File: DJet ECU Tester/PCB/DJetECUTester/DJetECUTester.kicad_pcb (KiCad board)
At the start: 2 copper layers, 93 x 60 mm, 101 parts, among them J1 ISP, J2 ECU, J3 USB_B_Mini, J4 BREAKOUT, J5 12V IN, J6 MPS, J7 VAC, J8 INJECTORS, Q1 MMBT2222ALT1G, Q10 MMBT2222ALT1G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

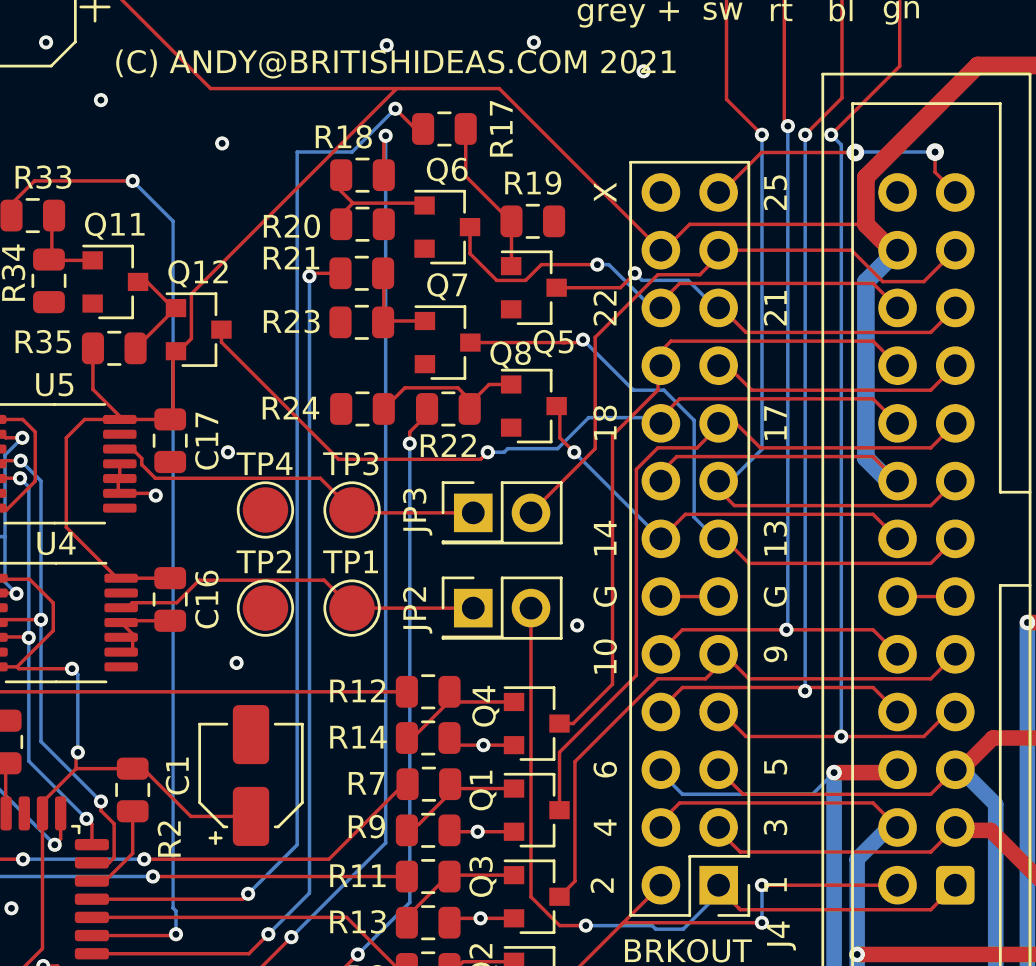
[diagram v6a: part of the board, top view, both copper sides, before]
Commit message: Added resistor to tester. Generated manufacturing files.
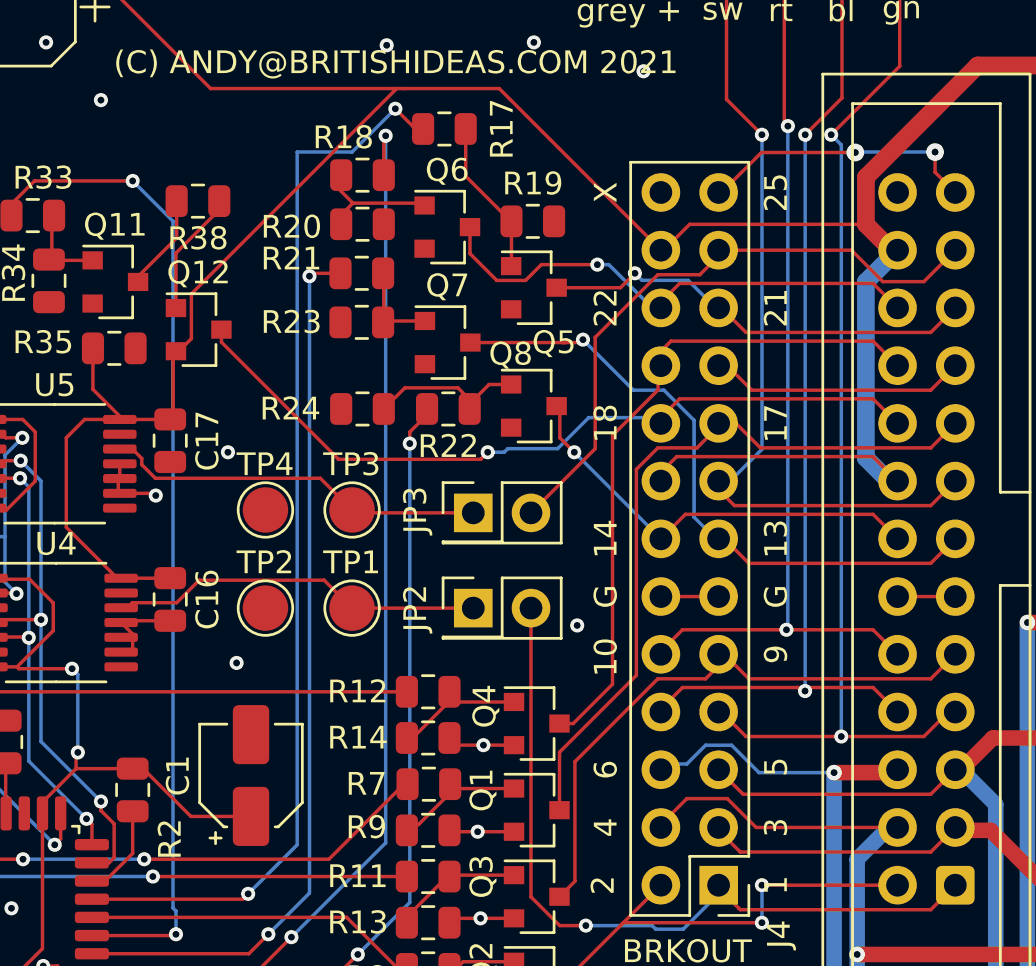
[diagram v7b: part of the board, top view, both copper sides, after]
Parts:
- added R38: 1k, Resistor_SMD:R_0805_2012Metric, F.Cu at (219.8, 83.9)
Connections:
- Q12 pad 1: Net-(Q11-Pad3) -> Net-(Q12-Pad1)
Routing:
- net Net-(Q12-Pad1): track 0.00 -> 4.93 mm
- net GND: vias 77 -> 76

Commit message: Working on version 1.1
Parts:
- removed JP1: RUN, Connector_PinHeader_2.54mm:PinHeader_1x02_P2.54mm_Vertical
- added J10: ECU3, Britishideas:PhoenixContact_COMBICON_PT_7, F.Cu at (264.0, 59.7)
- added J9: ECU2, Britishideas:PhoenixContact_COMBICON_PT_10, F.Cu at (228.9, 59.7)
- J2: value ECU -> ECU1; footprint Connector_IDC:IDC-Header_2x13_P2.54mm_Vertical -> Britishideas:PhoenixContact_COMBICON_PT_8
- J5: footprint TerminalBlock_TE-Connectivity:TerminalBlock_TE_282834-2_1x02_P2.54mm_Horizontal -> Britishideas:PhoenixContact_COMBICON_MKDSN_2
- J6: footprint TerminalBlock_TE-Connectivity:TerminalBlock_TE_282834-4_1x04_P2.54mm_Horizontal -> Britishideas:PhoenixContact_COMBICON_PT_4
- J8: footprint TerminalBlock_TE-Connectivity:TerminalBlock_TE_282834-8_1x08_P2.54mm_Horizontal -> Britishideas:PhoenixContact_COMBICON_PT_5
- moved J6 59.5 mm to (238.4, 129.2)
- moved J2 29.6 mm to (262.0, 85.8), turned to 270 degrees
- moved TP5 27.9 mm to (252.0, 95.9), turned to 270 degrees
- moved TP6 22.0 mm to (252.0, 101.0), turned to 270 degrees
- moved J8 21.6 mm to (244.2, 129.2), turned to 0 degrees
- moved TP7 16.8 mm to (252.0, 105.9), turned to 270 degrees
- moved TP8 13.1 mm to (251.9, 110.7), turned to 270 degrees
- moved TP9 11.8 mm to (251.9, 115.8), turned to 270 degrees
- moved J5 1.65 mm to (262.5, 72.5), turned to 270 degrees
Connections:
- net /CSV renamed /START
- net /ECU_INJGROUP1 renamed /ECU_INJGROUP1-3
- J2 pad 1: /ECU_AIRTEMP -> +12V
- J2 pad 2: /ECU_TPSWOT -> +12V
- J2 pad 4: /ECU_INJGROUP2 -> /ECU_INJGROUP2-4
- J2 pad 5: /ECU_INJGROUP3 -> /ECU_INJGROUP3-5
- J2 pad 6: /ECU_INJGROUP4 -> /ECU_INJGROUP4-6
- J2 pad 7: /MPS-7 -> GND
- J2 pad 8: /MPS-8 -> GND
- J4 pad 1: /ECU_AIRTEMP -> /ECU_AIRTEMP-1
- J4 pad 13: /ECU_TRIGGERGROUP2 -> /ECU_TRIGGERGROUP2-13
- J4 pad 14: /ECU_TRIGGERGROUP4 -> /ECU_TRIGGERGROUP4-14
- J4 pad 17: /ECU_TPSIDLE -> /ECU_TPSIDLE-17
- J4 pad 18: /ECU_COLDSTARTRELAY -> /ECU_START-18
- J4 pad 19: /ECU_FUELPUMPRELAY -> /ECU_FUELPUMPRELAY-19
- J4 pad 2: /ECU_TPSWOT -> /ECU_TPSWOT-2
- J4 pad 20: /ECU_TPSACCEL2 -> /ECU_TPSACCEL2-20
- J4 pad 21: /ECU_TRIGGERGROUP1 -> /ECU_TRIGGERGROUP1-21
- J4 pad 22: /ECU_TRIGGERGROUP3 -> /ECU_TRIGGERGROUP3-22
- J4 pad 23: /ECU_COOLANTTEMP -> /ECU_COOLANTTEMP-23
- J4 pad 25: /ECU_DIAGGROUP13 -> /ECU_DIAGGROUP13-25
- J4 pad 4: /ECU_INJGROUP2 -> /ECU_INJGROUP2-4
- J4 pad 5: /ECU_INJGROUP3 -> /ECU_INJGROUP3-5
- J4 pad 6: /ECU_INJGROUP4 -> /ECU_INJGROUP4-6
- J4 pad 9: /ECU_TPSACCEL1 -> /ECU_TPSACCEL1-9
- J5 pad 1: +12V -> GND
- J5 pad 2: GND -> +12V
- J8 pad 2: GND -> /ECU_INJGROUP2-4
- J8 pad 3: /ECU_INJGROUP2 -> /ECU_INJGROUP3-5
- J8 pad 4: GND -> /ECU_INJGROUP4-6
- J8 pad 5: /ECU_INJGROUP3 -> GND
- JP2 pad 2: /ECU_AIRTEMP -> /ECU_AIRTEMP-1
- JP3 pad 2: /ECU_COOLANTTEMP -> /ECU_COOLANTTEMP-23
- Q1 pad 3: /ECU_TPSIDLE -> /ECU_TPSIDLE-17
- Q12 pad 3: /ECU_COLDSTARTRELAY -> /ECU_START-18
- Q2 pad 3: /ECU_TPSWOT -> /ECU_TPSWOT-2
- Q3 pad 3: /ECU_TPSACCEL1 -> /ECU_TPSACCEL1-9
- Q4 pad 3: /ECU_TPSACCEL2 -> /ECU_TPSACCEL2-20
- Q5 pad 3: /ECU_TRIGGERGROUP1 -> /ECU_TRIGGERGROUP1-21
- Q6 pad 3: /ECU_TRIGGERGROUP3 -> /ECU_TRIGGERGROUP3-22
- Q7 pad 3: /ECU_TRIGGERGROUP2 -> /ECU_TRIGGERGROUP2-13
- Q8 pad 3: /ECU_TRIGGERGROUP4 -> /ECU_TRIGGERGROUP4-14
- TP6 pad 1: /ECU_INJGROUP2 -> /ECU_INJGROUP2-4
- TP7 pad 1: /ECU_INJGROUP3 -> /ECU_INJGROUP3-5
- TP8 pad 1: /ECU_INJGROUP4 -> /ECU_INJGROUP4-6
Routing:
- net +12V: track 182.9 -> 126.5 mm
- net /ECU_INJGROUP4: track 54.7 -> 0.00 mm, vias 4 -> 0
- net /ECU_INJGROUP1-3: track 51.2 -> 0.00 mm
- net /MPS-7: track 48.9 -> 0.00 mm, vias 2 -> 0
- net /MPS-8: track 46.8 -> 0.00 mm, vias 2 -> 0
- net /MPS-10: track 42.6 -> 0.00 mm, vias 2 -> 0
- net /ECU_INJGROUP2: track 40.8 -> 0.00 mm, vias 4 -> 0
- net /MPS-15: track 37.5 -> 0.00 mm, vias 1 -> 0
- net /ECU_INJGROUP3: track 36.4 -> 0.00 mm, vias 1 -> 0
- net /ECU_COLDSTARTRELAY: track 34.0 -> 0.00 mm, vias 1 -> 0
- net /ECU_AIRTEMP: track 33.3 -> 0.00 mm, vias 1 -> 0
- net /ECU_TPSIDLE: track 31.7 -> 0.00 mm
- net /ECU_TPSACCEL2: track 28.7 -> 0.00 mm
- net /ECU_TRIGGERGROUP2: track 27.4 -> 0.00 mm, vias 1 -> 0
- net /ECU_COOLANTTEMP: track 27.2 -> 0.00 mm
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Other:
- board size 93 x 60 mm -> 93 x 79 mm
- board text added: "(10)"
- board text added: "(15)"
- board text added: "(7)"
- board text added: "(8)"
- board text added: "11"
- board text added: "12"
- board text added: "15"
- board text added: "16"
- board text added: "19"
- board text added: "20"
- board text added: "23"
- board text added: "24"
- board text added: "7"
- board text added: "8"
- board text added: "I"
- board text added: "II"
- board text added: "III"
- board text added: "IV"
- board text added: "MERCEDES V8 DJET ECU TESTER V1.1"
- board text removed: "INJ1"
- board text removed: "INJ2"
- board text removed: "INJ3"
- board text removed: "INJ4"
- board text removed: "MERCEDES V8 DJET ECU TESTER V1"
